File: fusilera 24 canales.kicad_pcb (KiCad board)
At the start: 4 copper layers, 123 x 191.1 mm, 289 parts, among them J1 +12V borne M6, J2 GND borne M5, Q1 MMBT2222A, Q101 MMBT2222A, Q102 MMBT2222A, Q103 MMBT2222A, Q104 MMBT2222A, Q105 MMBT2222A, Q106 MMBT2222A, Q107 MMBT2222A, Q108 MMBT2222A, Q2 MMBT2222A, Q201 MMBT2222A, Q202 MMBT2222A, Q203 MMBT2222A, Q204 MMBT2222A, Q205 MMBT2222A, Q206 MMBT2222A, Q207 MMBT2222A, Q208 MMBT2222A, Q3 MMBT2222A, Q4 MMBT2222A, Q5 MMBT2222A, Q6 MMBT2222A, Q7 MMBT2222A, Q8 MMBT2222A, U1 LM339D, U10 BTS50010-1TAD, U101 LM339D, U102 74HC132D, U103 BTS50010-1TAD, U108 BTS50010-1TAD, U109 74HC132D, U11 BTS50010-1TAD, U110 BTS50010-1TAD, U111 BTS50010-1TAD, U2 74HC132D, U201 LM339D, U202 74HC132D, U203 BTS50010-1TAD, U208 BTS50010-1TAD, U209 74HC132D, U210 BTS50010-1TAD, U211 BTS50010-1TAD, U3 BTS50010-1TAD, U4 MCP23017-E/SO, U5 MCP23017-E/SO, U6 LM5164DDA, U7 AP2112K-3.3, U8 BTS50010-1TAD, U9 74HC132D

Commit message: Une al plano las islas de +3,3 V de la Celda2 con puentes en B.Cu
Los pads de U101 pin 3, U102 pin 14 y sus resistencias y condensadores de
+3,3 V quedaban en islas de In2 encerradas por las pistas del bus hacia el
controlador, sin conexión física al plano principal (el DRC de KiCad no lo
detecta). Se añaden dos puentes de 0,5 mm en B.Cu y se anota el hallazgo en
CONTEXTO_PROYECTO.md.
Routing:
- net +3.3V: track 180.3 -> 196.4 mm

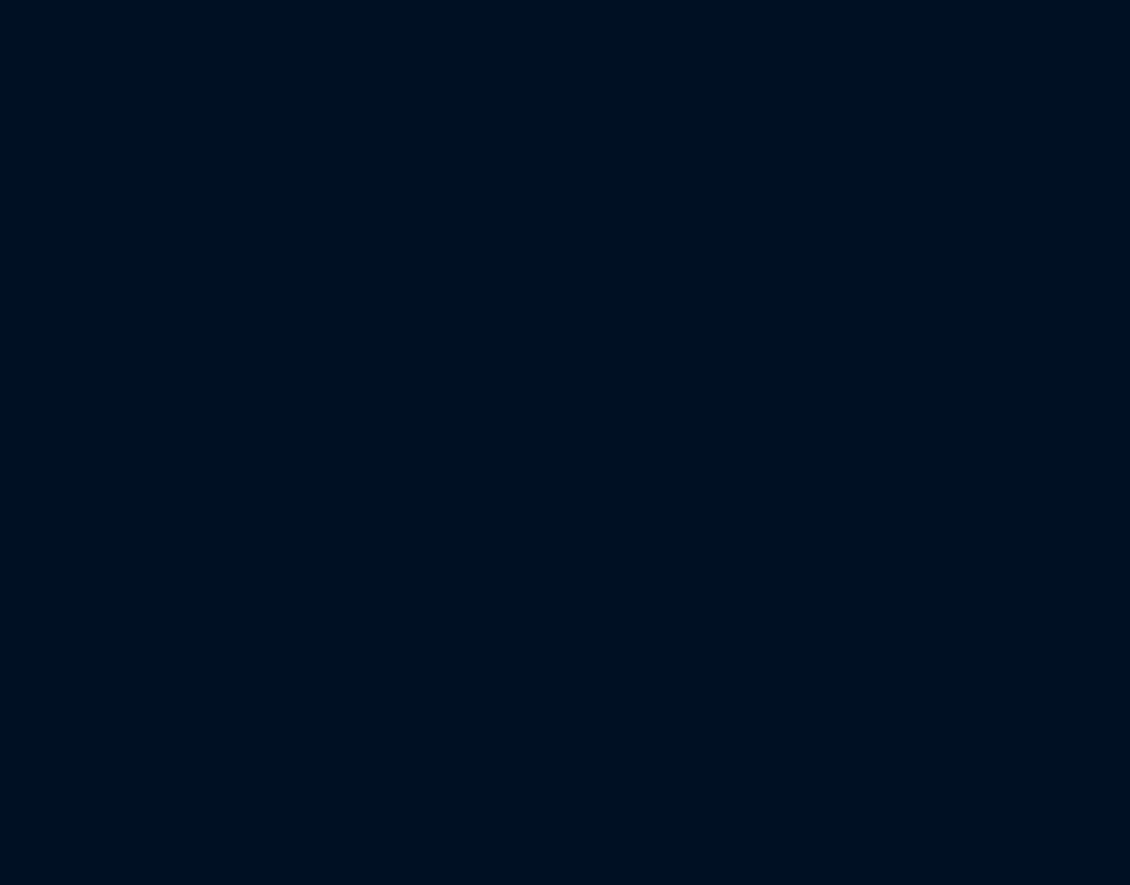
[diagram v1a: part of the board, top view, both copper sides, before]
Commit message: Añade las celdas 4 y 5 de la cara inferior como copias volteadas en B.Cu
Agrega las hojas Celda4 y Celda5 al esquemático raíz (referencias +300 y +400,
pines sin cablear) y crea sus 87 footprints cada una en B.Cu como imagen en
espejo de la celda dorada, con 556 pistas y 101 vías, aparcadas bajo el
contorno. Con las siete celdas previstas (3 en la cara frontal, 4 en la
inferior) quedan 28 canales: el cuarto canal de la Celda5 y las celdas 6 y 7
serán las salidas directas. Se documenta el plan en CONTEXTO_PROYECTO.md.
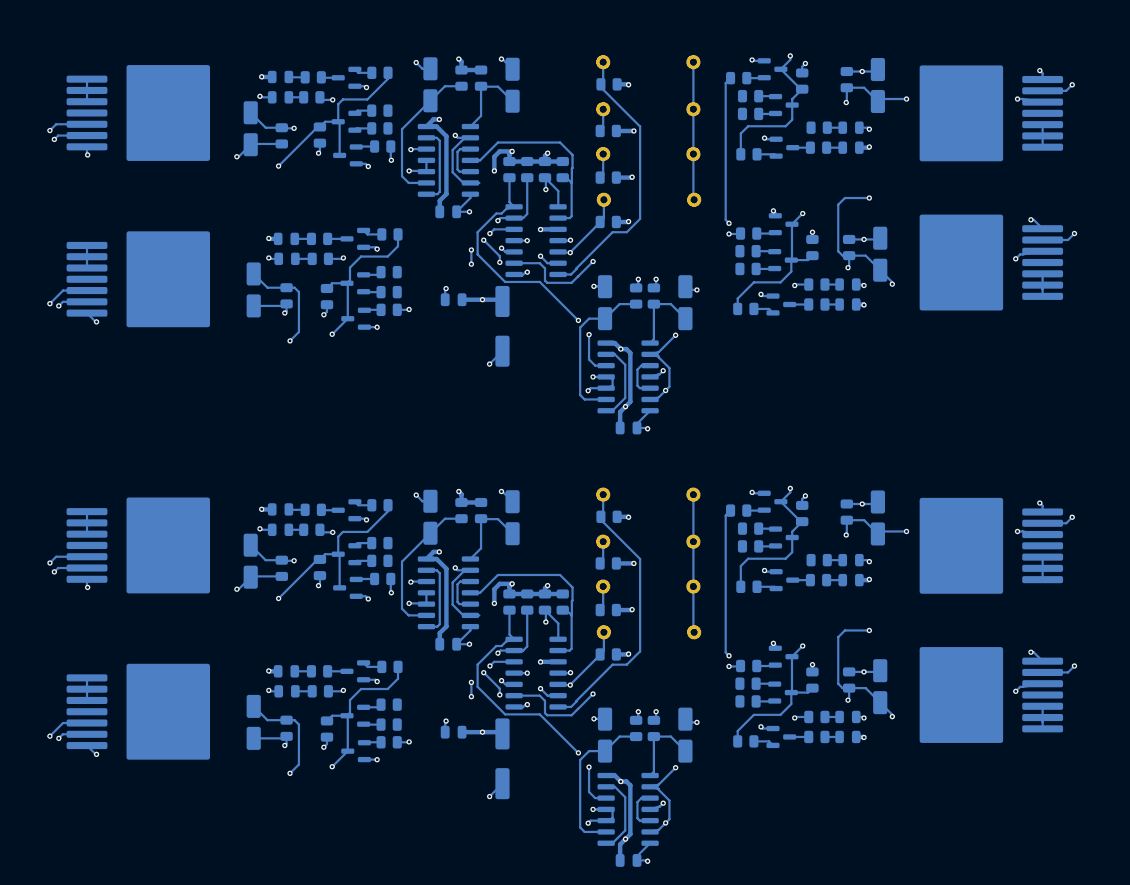
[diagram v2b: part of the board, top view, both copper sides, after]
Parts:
- added C301: 100uF 16V, Capacitor_SMD:CP_Elec_6.3x5.4, B.Cu at (-115.1, 266.3)
- added C302: 100nF, Capacitor_SMD:C_0805_2012Metric, B.Cu at (-120.6, 263.3)
- added C303: 1uF 25V, Capacitor_SMD:CP_Elec_4x5.4, B.Cu at (-114.0, 239.1)
- added C304: 100nF, Capacitor_SMD:C_0805_2012Metric, B.Cu at (-121.3, 253.4)
- added C305: 1uF 25V, Capacitor_SMD:CP_Elec_4x5.4, B.Cu at (-143.5, 244.0)
- added C316: 1uF 25V, Capacitor_SMD:CP_Elec_4x5.4, B.Cu at (-143.2, 262.2)
- added C317: 1uF 25V, Capacitor_SMD:CP_Elec_4x5.4, B.Cu at (-123.3, 239.1)
- added C318: 1uF 25V, Capacitor_SMD:CP_Elec_4x5.4, B.Cu at (-103.6, 263.6)
- added C319: 1uF 25V, Capacitor_SMD:CP_Elec_4x5.4, B.Cu at (-94.5, 263.6)
- added C320: 100nF, Capacitor_SMD:C_0805_2012Metric, B.Cu at (-100.9, 277.7)
- added C321: 1uF 25V, Capacitor_SMD:CP_Elec_4x5.4, B.Cu at (-72.6, 258.2)
- added C322: 1uF 25V, Capacitor_SMD:CP_Elec_4x5.4, B.Cu at (-72.9, 239.2)
- added C401: 100uF 16V, Capacitor_SMD:CP_Elec_6.3x5.4, B.Cu at (-115.1, 315.0)
- added C402: 100nF, Capacitor_SMD:C_0805_2012Metric, B.Cu at (-120.6, 312.0)
- added C403: 1uF 25V, Capacitor_SMD:CP_Elec_4x5.4, B.Cu at (-114.0, 287.8)
- added C404: 100nF, Capacitor_SMD:C_0805_2012Metric, B.Cu at (-121.3, 302.1)
- added C405: 1uF 25V, Capacitor_SMD:CP_Elec_4x5.4, B.Cu at (-143.5, 292.7)
- added C416: 1uF 25V, Capacitor_SMD:CP_Elec_4x5.4, B.Cu at (-143.2, 310.9)
- added C417: 1uF 25V, Capacitor_SMD:CP_Elec_4x5.4, B.Cu at (-123.3, 287.8)
- added C418: 1uF 25V, Capacitor_SMD:CP_Elec_4x5.4, B.Cu at (-103.6, 312.3)
- added C419: 1uF 25V, Capacitor_SMD:CP_Elec_4x5.4, B.Cu at (-94.5, 312.3)
- added C420: 100nF, Capacitor_SMD:C_0805_2012Metric, B.Cu at (-100.9, 326.4)
- added C421: 1uF 25V, Capacitor_SMD:CP_Elec_4x5.4, B.Cu at (-72.6, 306.9)
- added C422: 1uF 25V, Capacitor_SMD:CP_Elec_4x5.4, B.Cu at (-72.9, 287.9)
- added D301: BAT54C, Package_TO_SOT_SMD:SOT-23, B.Cu at (-132.7, 243.2)
- added D302: LED verde, LED_SMD:LED_0805_2012Metric, B.Cu at (-140.1, 238.2)
- added D303: LED rojo, LED_SMD:LED_0805_2012Metric, B.Cu at (-140.1, 240.5)
- added D307: LED verde, LED_SMD:LED_0805_2012Metric, B.Cu at (-139.5, 256.4)
- added D308: BAT54C, Package_TO_SOT_SMD:SOT-23, B.Cu at (-131.7, 261.4)
- added D309: LED rojo, LED_SMD:LED_0805_2012Metric, B.Cu at (-139.4, 258.7)
- added D310: LED rojo, LED_SMD:LED_0805_2012Metric, B.Cu at (-76.2, 261.6)
- added D311: LED rojo, LED_SMD:LED_0805_2012Metric, B.Cu at (-75.9, 243.9)
- added D312: LED verde, LED_SMD:LED_0805_2012Metric, B.Cu at (-76.2, 263.8)
- added D313: LED verde, LED_SMD:LED_0805_2012Metric, B.Cu at (-75.9, 246.2)
- added D314: BAT54C, Package_TO_SOT_SMD:SOT-23, B.Cu at (-83.5, 258.8)
- added D315: BAT54C, Package_TO_SOT_SMD:SOT-23, B.Cu at (-83.5, 241.4)
- added D401: BAT54C, Package_TO_SOT_SMD:SOT-23, B.Cu at (-132.7, 291.9)
- added D402: LED verde, LED_SMD:LED_0805_2012Metric, B.Cu at (-140.1, 286.9)
- added D403: LED rojo, LED_SMD:LED_0805_2012Metric, B.Cu at (-140.1, 289.2)
- added D407: LED verde, LED_SMD:LED_0805_2012Metric, B.Cu at (-139.5, 305.1)
- added D408: BAT54C, Package_TO_SOT_SMD:SOT-23, B.Cu at (-131.7, 310.1)
- added D409: LED rojo, LED_SMD:LED_0805_2012Metric, B.Cu at (-139.4, 307.4)
- added D410: LED rojo, LED_SMD:LED_0805_2012Metric, B.Cu at (-76.2, 310.3)
- added D411: LED rojo, LED_SMD:LED_0805_2012Metric, B.Cu at (-75.9, 292.6)
- added D412: LED verde, LED_SMD:LED_0805_2012Metric, B.Cu at (-76.2, 312.5)
- added D413: LED verde, LED_SMD:LED_0805_2012Metric, B.Cu at (-75.9, 294.9)
- added D414: BAT54C, Package_TO_SOT_SMD:SOT-23, B.Cu at (-83.5, 307.5)
- added D415: BAT54C, Package_TO_SOT_SMD:SOT-23, B.Cu at (-83.5, 290.1)
- added Q301: MMBT2222A, Package_TO_SOT_SMD:SOT-23, B.Cu at (-132.7, 238.3)
- added Q302: MMBT2222A, Package_TO_SOT_SMD:SOT-23, B.Cu at (-132.5, 247.0)
- added Q303: MMBT2222A, Package_TO_SOT_SMD:SOT-23, B.Cu at (-131.7, 256.4)
- added Q304: MMBT2222A, Package_TO_SOT_SMD:SOT-23, B.Cu at (-131.6, 265.4)
- added Q305: MMBT2222A, Package_TO_SOT_SMD:SOT-23, B.Cu at (-83.5, 254.8)
- added Q306: MMBT2222A, Package_TO_SOT_SMD:SOT-23, B.Cu at (-84.7, 237.3)
- added Q307: MMBT2222A, Package_TO_SOT_SMD:SOT-23, B.Cu at (-83.7, 263.8)
- added Q308: MMBT2222A, Package_TO_SOT_SMD:SOT-23, B.Cu at (-83.4, 246.2)
- added Q401: MMBT2222A, Package_TO_SOT_SMD:SOT-23, B.Cu at (-132.7, 287.0)
- added Q402: MMBT2222A, Package_TO_SOT_SMD:SOT-23, B.Cu at (-132.5, 295.7)
- added Q403: MMBT2222A, Package_TO_SOT_SMD:SOT-23, B.Cu at (-131.7, 305.1)
- added Q404: MMBT2222A, Package_TO_SOT_SMD:SOT-23, B.Cu at (-131.6, 314.1)
- added Q405: MMBT2222A, Package_TO_SOT_SMD:SOT-23, B.Cu at (-83.5, 303.5)
- added Q406: MMBT2222A, Package_TO_SOT_SMD:SOT-23, B.Cu at (-84.7, 286.0)
- added Q407: MMBT2222A, Package_TO_SOT_SMD:SOT-23, B.Cu at (-83.7, 312.5)
- added Q408: MMBT2222A, Package_TO_SOT_SMD:SOT-23, B.Cu at (-83.4, 294.9)
- added R301: umbral, Resistor_THT:R_Axial_DIN0207_L6.3mm_D2.5mm_P10.16mm_Horizontal, B.Cu at (-93.6, 252.0)
- added R302: 10k, Resistor_SMD:R_0805_2012Metric, B.Cu at (-103.2, 254.5)
- added R303: 10k, Resistor_SMD:R_0805_2012Metric, B.Cu at (-108.4, 248.6)
- added R304: 4.7k, Resistor_SMD:R_0805_2012Metric, B.Cu at (-128.9, 244.0)
- added R305: 4.7k, Resistor_SMD:R_0805_2012Metric, B.Cu at (-128.9, 242.0)
- added R306: 10k, Resistor_SMD:R_0805_2012Metric, B.Cu at (-117.6, 238.3)
- added R307: 100k, Resistor_SMD:R_0805_2012Metric, B.Cu at (-128.9, 237.7)
- added R308: 100k, Resistor_SMD:R_0805_2012Metric, B.Cu at (-135.7, 244.7)
- added R309: 1k, Resistor_SMD:R_0805_2012Metric, B.Cu at (-140.0, 244.8)
- added R310: 2.2k, Resistor_SMD:R_0805_2012Metric, B.Cu at (-136.4, 238.2)
- added R311: 4.7k, Resistor_SMD:R_0805_2012Metric, B.Cu at (-128.6, 246.0)
- added R312: 1k, Resistor_SMD:R_0805_2012Metric, B.Cu at (-136.6, 240.5)
- added R319: 4.7k, Resistor_SMD:R_0805_2012Metric, B.Cu at (-127.9, 262.4)
- added R320: 4.7k, Resistor_SMD:R_0805_2012Metric, B.Cu at (-127.9, 260.2)
- added R321: 2.2k, Resistor_SMD:R_0805_2012Metric, B.Cu at (-135.7, 256.4)
- added R322: 100k, Resistor_SMD:R_0805_2012Metric, B.Cu at (-127.8, 255.9)
- added R323: 100k, Resistor_SMD:R_0805_2012Metric, B.Cu at (-134.9, 262.9)
- added R324: 1k, Resistor_SMD:R_0805_2012Metric, B.Cu at (-139.5, 262.8)
- added R325: 1k, Resistor_SMD:R_0805_2012Metric, B.Cu at (-135.7, 258.7)
- added R326: 4.7k, Resistor_SMD:R_0805_2012Metric, B.Cu at (-127.9, 264.4)
- added R327: 10k, Resistor_SMD:R_0805_2012Metric, B.Cu at (-110.4, 248.6)
- added R328: 10k, Resistor_SMD:R_0805_2012Metric, B.Cu at (-119.8, 238.3)
- added R329: umbral, Resistor_THT:R_Axial_DIN0207_L6.3mm_D2.5mm_P10.16mm_Horizontal, B.Cu at (-93.6, 236.5)
- added R330: 10k, Resistor_SMD:R_0805_2012Metric, B.Cu at (-103.1, 239.0)
- added R331: 10k, Resistor_SMD:R_0805_2012Metric, B.Cu at (-100.1, 262.9)
- added R332: 10k, Resistor_SMD:R_0805_2012Metric, B.Cu at (-98.1, 262.9)
- added R333: 1k, Resistor_SMD:R_0805_2012Metric, B.Cu at (-79.7, 261.6)
- added R334: 1k, Resistor_SMD:R_0805_2012Metric, B.Cu at (-79.5, 243.9)
- added R335: 4.7k, Resistor_SMD:R_0805_2012Metric, B.Cu at (-87.4, 255.8)
- added R336: 4.7k, Resistor_SMD:R_0805_2012Metric, B.Cu at (-88.5, 238.3)
- added R337: 4.7k, Resistor_SMD:R_0805_2012Metric, B.Cu at (-87.5, 257.8)
- added R338: 4.7k, Resistor_SMD:R_0805_2012Metric, B.Cu at (-87.5, 259.8)
- added R339: 4.7k, Resistor_SMD:R_0805_2012Metric, B.Cu at (-87.2, 240.4)
- added R340: 4.7k, Resistor_SMD:R_0805_2012Metric, B.Cu at (-87.2, 242.4)
- added R341: 2.2k, Resistor_SMD:R_0805_2012Metric, B.Cu at (-79.7, 263.8)
- added R342: 2.2k, Resistor_SMD:R_0805_2012Metric, B.Cu at (-79.5, 246.2)
- added R343: 100k, Resistor_SMD:R_0805_2012Metric, B.Cu at (-87.7, 264.3)
- added R344: 100k, Resistor_SMD:R_0805_2012Metric, B.Cu at (-80.2, 257.4)
- added R345: 100k, Resistor_SMD:R_0805_2012Metric, B.Cu at (-87.4, 246.9)
- added R346: 100k, Resistor_SMD:R_0805_2012Metric, B.Cu at (-81.4, 238.7)
- added R347: 1k, Resistor_SMD:R_0805_2012Metric, B.Cu at (-76.1, 257.4)
- added R348: 1k, Resistor_SMD:R_0805_2012Metric, B.Cu at (-76.4, 238.5)
- added R349: umbral, Resistor_THT:R_Axial_DIN0207_L6.3mm_D2.5mm_P10.16mm_Horizontal, B.Cu at (-93.6, 241.8)
- added R350: 10k, Resistor_SMD:R_0805_2012Metric, B.Cu at (-103.2, 244.3)
- added R351: umbral, Resistor_THT:R_Axial_DIN0207_L6.3mm_D2.5mm_P10.16mm_Horizontal, B.Cu at (-93.6, 246.9)
- added R352: 10k, Resistor_SMD:R_0805_2012Metric, B.Cu at (-103.2, 249.5)
- added R353: 10k, Resistor_SMD:R_0805_2012Metric, B.Cu at (-112.4, 248.6)
- added R354: 10k, Resistor_SMD:R_0805_2012Metric, B.Cu at (-114.4, 248.6)
- added R401: umbral, Resistor_THT:R_Axial_DIN0207_L6.3mm_D2.5mm_P10.16mm_Horizontal, B.Cu at (-93.6, 300.7)
- added R402: 10k, Resistor_SMD:R_0805_2012Metric, B.Cu at (-103.2, 303.2)
- added R403: 10k, Resistor_SMD:R_0805_2012Metric, B.Cu at (-108.4, 297.3)
- added R404: 4.7k, Resistor_SMD:R_0805_2012Metric, B.Cu at (-128.9, 292.7)
- added R405: 4.7k, Resistor_SMD:R_0805_2012Metric, B.Cu at (-128.9, 290.7)
- added R406: 10k, Resistor_SMD:R_0805_2012Metric, B.Cu at (-117.6, 287.0)
- added R407: 100k, Resistor_SMD:R_0805_2012Metric, B.Cu at (-128.9, 286.4)
- added R408: 100k, Resistor_SMD:R_0805_2012Metric, B.Cu at (-135.7, 293.4)
- added R409: 1k, Resistor_SMD:R_0805_2012Metric, B.Cu at (-140.0, 293.5)
- added R410: 2.2k, Resistor_SMD:R_0805_2012Metric, B.Cu at (-136.4, 286.9)
- added R411: 4.7k, Resistor_SMD:R_0805_2012Metric, B.Cu at (-128.6, 294.7)
- added R412: 1k, Resistor_SMD:R_0805_2012Metric, B.Cu at (-136.6, 289.2)
- added R419: 4.7k, Resistor_SMD:R_0805_2012Metric, B.Cu at (-127.9, 311.1)
- added R420: 4.7k, Resistor_SMD:R_0805_2012Metric, B.Cu at (-127.9, 308.9)
- added R421: 2.2k, Resistor_SMD:R_0805_2012Metric, B.Cu at (-135.7, 305.1)
- added R422: 100k, Resistor_SMD:R_0805_2012Metric, B.Cu at (-127.8, 304.6)
- added R423: 100k, Resistor_SMD:R_0805_2012Metric, B.Cu at (-134.9, 311.6)
- added R424: 1k, Resistor_SMD:R_0805_2012Metric, B.Cu at (-139.5, 311.5)
- added R425: 1k, Resistor_SMD:R_0805_2012Metric, B.Cu at (-135.7, 307.4)
- added R426: 4.7k, Resistor_SMD:R_0805_2012Metric, B.Cu at (-127.9, 313.1)
- added R427: 10k, Resistor_SMD:R_0805_2012Metric, B.Cu at (-110.4, 297.3)
- added R428: 10k, Resistor_SMD:R_0805_2012Metric, B.Cu at (-119.8, 287.0)
- added R429: umbral, Resistor_THT:R_Axial_DIN0207_L6.3mm_D2.5mm_P10.16mm_Horizontal, B.Cu at (-93.6, 285.2)
- added R430: 10k, Resistor_SMD:R_0805_2012Metric, B.Cu at (-103.1, 287.7)
- added R431: 10k, Resistor_SMD:R_0805_2012Metric, B.Cu at (-100.1, 311.6)
- added R432: 10k, Resistor_SMD:R_0805_2012Metric, B.Cu at (-98.1, 311.6)
- added R433: 1k, Resistor_SMD:R_0805_2012Metric, B.Cu at (-79.7, 310.3)
- added R434: 1k, Resistor_SMD:R_0805_2012Metric, B.Cu at (-79.5, 292.6)
- added R435: 4.7k, Resistor_SMD:R_0805_2012Metric, B.Cu at (-87.4, 304.5)
- added R436: 4.7k, Resistor_SMD:R_0805_2012Metric, B.Cu at (-88.5, 287.0)
- added R437: 4.7k, Resistor_SMD:R_0805_2012Metric, B.Cu at (-87.5, 306.5)
- added R438: 4.7k, Resistor_SMD:R_0805_2012Metric, B.Cu at (-87.5, 308.5)
- added R439: 4.7k, Resistor_SMD:R_0805_2012Metric, B.Cu at (-87.2, 289.1)
- added R440: 4.7k, Resistor_SMD:R_0805_2012Metric, B.Cu at (-87.2, 291.1)
- added R441: 2.2k, Resistor_SMD:R_0805_2012Metric, B.Cu at (-79.7, 312.5)
- added R442: 2.2k, Resistor_SMD:R_0805_2012Metric, B.Cu at (-79.5, 294.9)
- added R443: 100k, Resistor_SMD:R_0805_2012Metric, B.Cu at (-87.7, 313.0)
- added R444: 100k, Resistor_SMD:R_0805_2012Metric, B.Cu at (-80.2, 306.1)
- added R445: 100k, Resistor_SMD:R_0805_2012Metric, B.Cu at (-87.4, 295.6)
- added R446: 100k, Resistor_SMD:R_0805_2012Metric, B.Cu at (-81.4, 287.4)
- added R447: 1k, Resistor_SMD:R_0805_2012Metric, B.Cu at (-76.1, 306.1)
- added R448: 1k, Resistor_SMD:R_0805_2012Metric, B.Cu at (-76.4, 287.2)
- added R449: umbral, Resistor_THT:R_Axial_DIN0207_L6.3mm_D2.5mm_P10.16mm_Horizontal, B.Cu at (-93.6, 290.5)
- added R450: 10k, Resistor_SMD:R_0805_2012Metric, B.Cu at (-103.2, 293.0)
- added R451: umbral, Resistor_THT:R_Axial_DIN0207_L6.3mm_D2.5mm_P10.16mm_Horizontal, B.Cu at (-93.6, 295.6)
- added R452: 10k, Resistor_SMD:R_0805_2012Metric, B.Cu at (-103.2, 298.2)
- added R453: 10k, Resistor_SMD:R_0805_2012Metric, B.Cu at (-112.4, 297.3)
- added R454: 10k, Resistor_SMD:R_0805_2012Metric, B.Cu at (-114.4, 297.3)
- added U301: LM339D, Package_SO:SOIC-14_3.9x8.7mm_P1.27mm, B.Cu at (-111.4, 256.6)
- added U302: 74HC132D, Package_SO:SOIC-14_3.9x8.7mm_P1.27mm, B.Cu at (-121.2, 247.6)
- added U303: BTS50010-1TAD, Package_TO_SOT_SMD:TO-263-7_TabPin4, B.Cu at (-154.3, 242.2)
- added U308: BTS50010-1TAD, Package_TO_SOT_SMD:TO-263-7_TabPin4, B.Cu at (-154.3, 261.0)
- added U309: 74HC132D, Package_SO:SOIC-14_3.9x8.7mm_P1.27mm, B.Cu at (-101.0, 272.0)
- added U310: BTS50010-1TAD, Package_TO_SOT_SMD:TO-263-7_TabPin4, B.Cu at (-62.0, 259.1)
- added U311: BTS50010-1TAD, Package_TO_SOT_SMD:TO-263-7_TabPin4, B.Cu at (-62.0, 242.3)
- added U401: LM339D, Package_SO:SOIC-14_3.9x8.7mm_P1.27mm, B.Cu at (-111.4, 305.3)
- added U402: 74HC132D, Package_SO:SOIC-14_3.9x8.7mm_P1.27mm, B.Cu at (-121.2, 296.3)
- added U403: BTS50010-1TAD, Package_TO_SOT_SMD:TO-263-7_TabPin4, B.Cu at (-154.3, 290.9)
- added U408: BTS50010-1TAD, Package_TO_SOT_SMD:TO-263-7_TabPin4, B.Cu at (-154.3, 309.7)
- added U409: 74HC132D, Package_SO:SOIC-14_3.9x8.7mm_P1.27mm, B.Cu at (-101.0, 320.7)
- added U410: BTS50010-1TAD, Package_TO_SOT_SMD:TO-263-7_TabPin4, B.Cu at (-62.0, 307.8)
- added U411: BTS50010-1TAD, Package_TO_SOT_SMD:TO-263-7_TabPin4, B.Cu at (-62.0, 291.0)
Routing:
- net GND: track 263.4 -> 421.6 mm, vias 123 -> 189
- net +3.3V: track 196.4 -> 317.6 mm, vias 57 -> 95
- net Net-(U401C--): track 0.00 -> 96.6 mm, vias 0 -> 7
- net Net-(U301C--): track 0.00 -> 96.6 mm, vias 0 -> 7
- net Net-(U301A--): track 0.00 -> 88.7 mm, vias 0 -> 3
- net Net-(U401A--): track 0.00 -> 88.7 mm, vias 0 -> 3
- net Net-(U401B--): track 0.00 -> 86.4 mm, vias 0 -> 3
- net Net-(U301B--): track 0.00 -> 86.4 mm, vias 0 -> 3
- net Net-(U301D--): track 0.00 -> 75.2 mm, vias 0 -> 4
- net Net-(U401D--): track 0.00 -> 75.2 mm, vias 0 -> 4
- net Net-(Q306-C): track 0.00 -> 56.8 mm, vias 0 -> 2
- net Net-(Q406-C): track 0.00 -> 56.8 mm, vias 0 -> 2
- net Net-(Q305-C): track 0.00 -> 55.8 mm, vias 0 -> 2
- net Net-(Q405-C): track 0.00 -> 55.8 mm, vias 0 -> 2
- net Net-(Q404-C): track 0.00 -> 55.6 mm, vias 0 -> 2
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
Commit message: Coloca y rutea las celdas 4 y 5 en B.Cu con vías conscientes de todas las capas
Las huellas de las celdas inferiores se legalizan contra las vías, THT y cobre
de las celdas de arriba; el ruteo usa B.Cu e In2 con vías solo donde las tres
capas están libres, sin vías en pad y con 0,3 mm frente al +12 V. Las islas del
plano +3,3 V que partían las pistas de In2 se unen al plano con puentes.
Quedan 4 conexiones sin rutear en la Celda4 y las tiras de +12 V inferiores.
Se documenta el estado y el conflicto del bloque de potencia en CONTEXTO_PROYECTO.md.
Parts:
- C10, C11, C12, C13, C14, C15, C7, C8, C9, D4, D5, D6, F2, L1, R13, R14, R15, R16, R17, R18, U5, U6, U7: moved to B.Cu
- moved F2 232.3 mm to (-102.2, 77.4), turned to 0 degrees
- moved D4 217.3 mm to (-94.7, 77.4), turned to 180 degrees
- moved C7 216.4 mm to (-94.2, 71.9), turned to 180 degrees
- moved C8 216.4 mm to (-94.2, 68.2), turned to 180 degrees
- moved R18 213.6 mm to (-92.8, 64.4)
- moved R15 209.6 mm to (-90.8, 64.4)
- moved R17 209.6 mm to (-90.8, 68.0)
- moved D5 202.3 mm to (-87.2, 78.4)
- moved R13 200.8 mm to (-86.4, 65.6)
- moved U6 199.5 mm to (-85.8, 70.6), turned to 0 degrees
- moved R14 196.3 mm to (-84.2, 65.6)
- moved C10 189.8 mm to (-80.9, 71.4)
- moved R16 189.8 mm to (-80.9, 67.7)
- moved C9 188.3 mm to (-80.2, 80.2)
- moved L1 179.8 mm to (-75.9, 69.4), turned to 0 degrees
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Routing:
- net +3.3V: track 317.6 -> 403.0 mm, vias 95 -> 112
- net Net-(U301D--): track 75.2 -> 24.4 mm, vias 4 -> 2
- net GND: track 421.6 -> 382.1 mm, vias 189 -> 201
- net Net-(R353-Pad1): track 39.4 -> 0.00 mm, vias 4 -> 0
- net Net-(U401D--): track 75.2 -> 110.0 mm, vias 4 -> 8
- net Net-(Q402-C): track 53.7 -> 79.2 mm, vias 2 -> 4
- net Net-(R453-Pad1): track 39.4 -> 63.5 mm, vias 4 -> 6
- net Net-(U301B--): track 86.4 -> 64.2 mm, vias 3 -> 4
- net Net-(U301D-+): track 27.0 -> 48.7 mm, vias 1 -> 4
- net Net-(D401-Pad2): track 1.98 -> 21.0 mm, vias 0 -> 4
- net Net-(U401B--): track 86.4 -> 67.8 mm, vias 3 -> 4
- net Net-(Q302-C): track 53.7 -> 72.2 mm
- net Net-(U301B-+): track 31.4 -> 49.1 mm, vias 0 -> 4
- net Net-(Q306-C): track 56.8 -> 40.8 mm
- net Net-(Q406-C): track 56.8 -> 40.8 mm
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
